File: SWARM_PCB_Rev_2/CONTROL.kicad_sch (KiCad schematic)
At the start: 52 parts

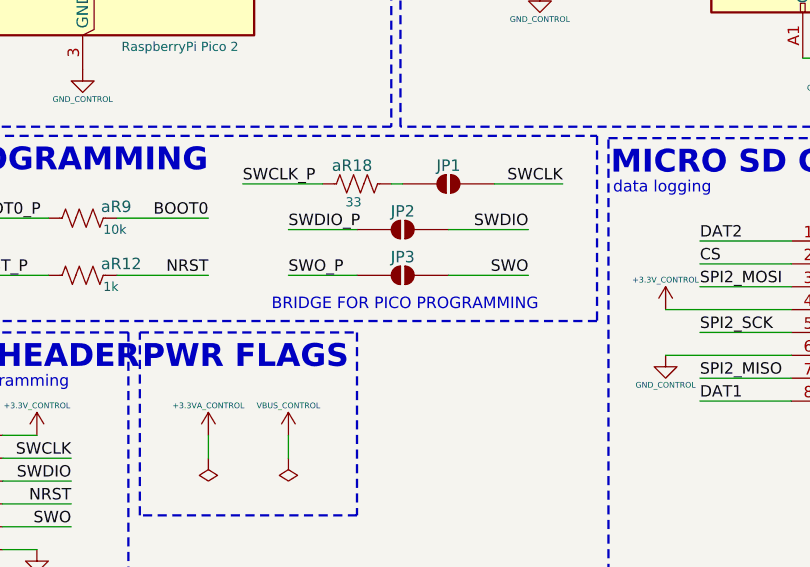
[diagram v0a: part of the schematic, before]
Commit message: Design review fixes: P7/P8/C10/C11/T4 + MPN audit
- P7: bR3 36k→4.3k, bR4 82k→4.3k (blue LEDs now 2.05mA each)
- P8: bD1 lib_id Diode:SS34→Device:D_TVS; embed D_TVS lib_symbol in POWER.kicad_sch
- C10: aR19 33Ω (RC0603FR-0733RL) added on SWO line (user-placed)
- C11: aFB1 footprint Resistor_SMD:R_0603_1608Metric→Inductor_SMD:L_0603_1608Metric
- T4: dD1/dD2 SS14-E3/61T bootstrap Schottky diodes added on HB_A/HB_B; MPN set
- BOM: MPNs added to J25–J28 (Samtec SSQ), aJ1/aJ4 (Harwin M50)
- DESIGN_REVIEW.md: close T4, T8/T9, P7, P8, C10, C11, H2, dC9, bL1/bL2 items

Co-Authored-By: Claude Sonnet 4.6 <noreply@anthropic.com>
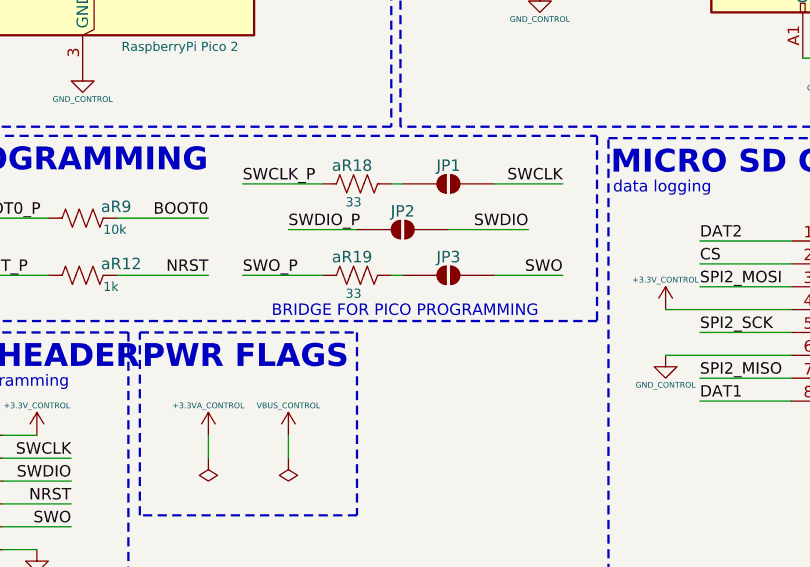
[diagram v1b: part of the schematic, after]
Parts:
- added aR19: 33, Resistor_SMD:R_0603_1608Metric, symbol Device:R_US
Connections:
- net SWO_P: now also aR19.2; no longer JP3.1 (A)
- new net: JP3.1 (A), aR19.1
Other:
- moved on the sheet: JP3
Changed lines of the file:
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@@
 	(text "BRIDGE FOR PICO PROGRAMMING\n"
 		(exclude_from_sim no)
-		(at 175.514 123.952 0)
+		(at 175.514 124.714 0)
 		(effects
 			(font
@@
 	(wire
 		(pts
+			(xy 173.99 120.65) (xy 175.26 120.65)
+		)
+		(stroke
+			(width 0)
+			(type default)
+		)
+	)
+	(wire
+		(pts
 			(xy 76.2 38.1) (xy 87.63 38.1)
 		)
@@
 	(wire
 		(pts
-			(xy 162.56 120.65) (xy 170.18 120.65)
+			(xy 157.48 120.65) (xy 166.37 120.65)
 		)
 		(stroke
@@
 	(wire
 		(pts
-			(xy 180.34 120.65) (xy 189.23 120.65)
+			(xy 185.42 120.65) (xy 193.04 120.65)
 		)
 		(stroke
@@
 	)
 	(label "SWO_P"
-		(at 162.56 120.65 0)
+		(at 157.48 120.65 0)
 		(effects
 			(font
@@
 	)
 	(label "SWO"
-		(at 189.23 120.65 180)
+		(at 193.04 120.65 180)
 		(effects
 			(font
@@
 	(symbol
 		(lib_id "Jumper:SolderJumper_2_Open")
-		(at 175.26 120.65 0)
+		(at 180.34 120.65 0)
 		(unit 1)
 		(body_style 1)
@@
 		(dnp no)
 		(property "Reference" "JP3"
-			(at 175.26 118.618 0)
+			(at 180.34 118.618 0)
 			(show_name no)
 			(do_not_autoplace no)
@@
 		)
 		(property "Value" "SolderJumper_2_Open"
-			(at 175.26 116.84 0)
+			(at 180.34 116.84 0)
 			(hide yes)
 			(show_name no)
@@
 		)
 		(property "Footprint" "Jumper:SolderJumper-2_P1.3mm_Open_TrianglePad1.0x1.5mm"
-			(at 175.26 120.65 0)
+			(at 180.34 120.65 0)
 			(hide yes)
 			(show_name no)
@@
 		)
 		(property "Datasheet" ""
-			(at 175.26 128.27 0)
+			(at 180.34 128.27 0)
 			(hide yes)
 			(show_name no)
@@
 		)
 		(property "Description" "Solder Jumper, 2-pole, open"
-			(at 175.26 125.73 0)
+			(at 180.34 125.73 0)
 			(hide yes)
 			(show_name no)
@@
 					(unit 1)
 				)
+			)
+		)
+	)
+	(symbol
+		(lib_id "Device:R_US")
+		(at 170.18 120.65 270)
+		(unit 1)
+		(body_style 1)
+		(exclude_from_sim no)
+		(in_bom yes)
+		(on_board yes)
+		(in_pos_files yes)
+		(dnp no)
+		(property "Reference" "aR19"
+			(at 167.386 118.618 90)
+			(show_name no)
+			(do_not_autoplace no)
+			(effects
+				(font
+					(size 1.27 1.27)
+				)
+				(justify left)
+			)
+		)
+		(property "Value" "33"
+			(at 168.91 122.682 90)
+			(show_name no)
+			(do_not_autoplace no)
+			(effects
+				(font
+					(size 1.016 1.016)
+					(color 22 0 255 1)
+				)
+				(justify left)
+			)
+		)
+		(property "Footprint" "Resistor_SMD:R_0603_1608Metric"
+			(at 169.926 121.666 90)
+			(hide yes)
+			(show_name no)
+			(do_not_autoplace no)
+			(effects
+				(font
+					(size 1.27 1.27)
+				)
+			)
+		)
+		(property "Datasheet" ""
+			(at 170.18 120.65 0)
+			(hide yes)
+			(show_name no)
+			(do_not_autoplace no)
+			(effects
+				(font
+					(size 1.27 1.27)
+				)
+			)
+		)
+		(property "Description" "Resistor, US symbol"
+			(at 170.18 120.65 0)
+			(hide yes)
+			(show_name no)
+			(do_not_autoplace no)
+			(effects
+				(font
+					(size 1.27 1.27)
+				)
+			)
+		)
+		(property "Manufacturer" "Yageo"
+			(at 30.48 6.35 0)
+			(hide yes)
+			(show_name no)
+			(do_not_autoplace no)
+			(effects
+				(font
+					(size 1.27 1.27)
+				)
+			)
+		)
+		(property "MPN" "RC0603FR-0733RL"
+			(at 30.48 6.35 0)
+			(hide yes)
+			(show_name no)
+			(do_not_autoplace no)
+			(effects
+				(font
+					(size 1.27 1.27)
+				)
+			)
+		)
+		(pin "2"
+		)
+		(pin "1"
+		)
+		(instances
+			(project "SWARM_PCB_Rev_2"
+				(path "/d61c6b76-225f-4e7b-954b-419fd350b2a8/0ec9a5b8-e6af-498c-b79e-09f97163fe47"
+					(reference "aR19")
+					(unit 1)
+				)
